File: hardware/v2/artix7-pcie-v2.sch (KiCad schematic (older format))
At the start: 43 parts, among them J10 USB_B_Micro, J3 JTAG_EN, J6 JTAG, J7 Conn_01x02, J8 SER, SW1 PROG, SW2 SW_SPST, U1 XC7A75T-FGG484, U2 W25Q64JVSSIM, U4 5P49V6965A000NLGI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

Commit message: v2 schematic/pcb progress commit - 12 unrouted
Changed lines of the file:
@@
 F13 "IO_L22_16_P" B R 10600 5300 50
 F14 "VCCO_16" I R 10600 5800 50
-F15 "IO_L23_16_N" B L 9350 5200 50
-F16 "IO_L23_16_P" B L 9350 5100 50
+F15 "IO_L9_16_N" B L 9350 5200 50
+F16 "IO_L9_16_P" B L 9350 5100 50
 $EndSheet
 Wire Wire Line
@@
 F40 "IO_L0_14" O R 10600 3850 50
 F41 "IO_L11_14_P" B L 9350 3750 50
-F42 "IO_L23_16_P" B L 9350 4750 50
-F43 "IO_L23_16_N" B L 9350 4650 50
+F42 "IO_L9_16_N" B L 9350 4650 50
+F43 "IO_L9_16_P" B L 9350 4750 50
 $EndSheet
 $Comp

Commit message: v2 hardware progress commit - fixed mounting holes and board edge
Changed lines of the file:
@@
 F19 "IO_L13_14_P" I R 10600 3150 50
 F20 "IO_L18_14_P" I L 9350 1600 50
-F21 "IO_L16_14_P" I R 10600 1600 50
-F22 "IO_L16_14_N" O R 10600 1500 50
-F23 "IO_L12_14_P" I R 10600 1800 50
-F24 "IO_L12_14_N" O R 10600 1700 50
-F25 "IO_L19_14_P" O L 9350 2900 50
-F26 "IO_L22_14_P" O L 9350 2700 50
-F27 "IO_L24_14_P" O L 9350 2500 50
-F28 "IO_L14_14_P" B L 9350 3550 50
-F29 "IO_L18_14_N" O L 9350 3250 50
-F30 "IO_L14_14_N" B L 9350 3650 50
-F31 "VCCO_14" I R 10600 2700 50
-F32 "VCCO_16" I R 10600 2800 50
-F33 "IO_L13_14_N" I R 10600 3250 50
-F34 "IO_L21_14_N" B R 10600 3550 50
-F35 "IO_L21_14_P" O R 10600 3450 50
-F36 "IO_L22_14_N" I L 9350 3950 50
-F37 "IO_L24_14_N" I L 9350 3850 50
-F38 "IO_L5_14_P" B R 10600 4150 50
-F39 "IO_L5_14_N" B R 10600 4050 50
-F40 "IO_L0_14" O R 10600 3850 50
-F41 "IO_L11_14_P" B L 9350 3750 50
-F42 "IO_L9_16_N" B L 9350 4650 50
-F43 "IO_L9_16_P" B L 9350 4750 50
+F21 "IO_L16_14_N" O R 10600 1500 50
+F22 "IO_L12_14_P" I R 10600 1800 50
+F23 "IO_L19_14_P" O L 9350 2900 50
+F24 "IO_L22_14_P" O L 9350 2700 50
+F25 "IO_L24_14_P" O L 9350 2500 50
+F26 "IO_L14_14_P" B L 9350 3550 50
+F27 "IO_L18_14_N" O L 9350 3250 50
+F28 "IO_L14_14_N" B L 9350 3650 50
+F29 "VCCO_14" I R 10600 2700 50
+F30 "VCCO_16" I R 10600 2800 50
+F31 "IO_L13_14_N" I R 10600 3250 50
+F32 "IO_L21_14_N" B R 10600 3550 50
+F33 "IO_L21_14_P" O R 10600 3450 50
+F34 "IO_L22_14_N" I L 9350 3950 50
+F35 "IO_L24_14_N" I L 9350 3850 50
+F36 "IO_L5_14_P" B R 10600 4150 50
+F37 "IO_L5_14_N" B R 10600 4050 50
+F38 "IO_L0_14" O R 10600 3850 50
+F39 "IO_L11_14_P" B L 9350 3750 50
+F40 "IO_L9_16_N" B L 9350 4650 50
+F41 "IO_L9_16_P" B L 9350 4750 50
+F42 "IO_L12_14_N" I R 10600 1700 50
+F43 "IO_L16_14_P" O R 10600 1600 50
 $EndSheet
 $Comp

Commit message: v2 hardware: J2 differential pairs tuned
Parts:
- SW2: value SW_SPST -> USER
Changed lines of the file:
@@
 P 8950 1800
 F 0 "SW2" H 8950 2035 50  0000 C CNN
-F 1 "SW_SPST" H 8950 1944 50  0000 C CNN
+F 1 "USER" H 8950 1944 50  0000 C CNN
 F 2 "tom-mechanical:SW_Push_1P1T_NO_CK_KMR2" H 8950 1800 50  0001 C CNN
 F 3 "~" H 8950 1800 50  0001 C CNN

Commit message: v2 hardware: j2_34 diff pairs matched, fix 0402 resistor packages, dropped paste from DNP resistors
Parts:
- R1, R10, R2, R29, R3, R30, R34, R35, R37, R4, R5, R51, R6, R7, R9: footprint tom-passives:C_0402_1005Metric -> tom-passives:R_0402_1005Metric
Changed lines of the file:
@@
 F 0 "R7" H 7971 1188 40  0000 L CNN
 F 1 "4.7k/5%" H 7971 1112 40  0000 L CNN
-F 2 "tom-passives:C_0402_1005Metric" V 7830 1150 30  0001 C CNN
+F 2 "tom-passives:R_0402_1005Metric" V 7830 1150 30  0001 C CNN
 F 3 "" H 7900 1150 30  0000 C CNN
 	1    7900 1150
@@
 F 0 "R6" H 6471 1088 40  0000 L CNN
 F 1 "2.4k/5%" H 6471 1012 40  0000 L CNN
-F 2 "tom-passives:C_0402_1005Metric" V 6330 1050 30  0001 C CNN
+F 2 "tom-passives:R_0402_1005Metric" V 6330 1050 30  0001 C CNN
 F 3 "" H 6400 1050 30  0000 C CNN
 	1    6400 1050
@@
 F 0 "R5" H 6071 988 40  0000 L CNN
 F 1 "4.7k/5%" H 6071 912 40  0000 L CNN
-F 2 "tom-passives:C_0402_1005Metric" V 5930 950 30  0001 C CNN
+F 2 "tom-passives:R_0402_1005Metric" V 5930 950 30  0001 C CNN
 F 3 "" H 6000 950 30  0000 C CNN
 	1    6000 950
@@
 F 0 "R3" H 5071 3088 40  0000 L CNN
 F 1 "4.7k/5%" H 5071 3012 40  0000 L CNN
-F 2 "tom-passives:C_0402_1005Metric" V 4930 3050 30  0001 C CNN
+F 2 "tom-passives:R_0402_1005Metric" V 4930 3050 30  0001 C CNN
 F 3 "" H 5000 3050 30  0000 C CNN
 	1    5000 3050
@@
 F 0 "R2" H 4671 2988 40  0000 L CNN
 F 1 "4.7k/5%" H 4671 2912 40  0000 L CNN
-F 2 "tom-passives:C_0402_1005Metric" V 4530 2950 30  0001 C CNN
+F 2 "tom-passives:R_0402_1005Metric" V 4530 2950 30  0001 C CNN
 F 3 "" H 4600 2950 30  0000 C CNN
 	1    4600 2950
@@
 F 0 "R1" H 4221 2888 40  0000 L CNN
 F 1 "1K/5%" H 4221 2812 40  0000 L CNN
-F 2 "tom-passives:C_0402_1005Metric" V 4080 2850 30  0001 C CNN
+F 2 "tom-passives:R_0402_1005Metric" V 4080 2850 30  0001 C CNN
 F 3 "" H 4150 2850 30  0000 C CNN
 	1    4150 2850
@@
 F 0 "R4" H 5921 2488 40  0000 L CNN
 F 1 "1k/5%" H 5921 2412 40  0000 L CNN
-F 2 "tom-passives:C_0402_1005Metric" V 5780 2450 30  0001 C CNN
+F 2 "tom-passives:R_0402_1005Metric" V 5780 2450 30  0001 C CNN
 F 3 "" H 5850 2450 30  0000 C CNN
 	1    5850 2450
@@
 F 0 "R30" V 8765 2500 40  0000 C CNN
 F 1 "1k/5%" V 8841 2500 40  0000 C CNN
-F 2 "tom-passives:C_0402_1005Metric" V 8880 2500 30  0001 C CNN
+F 2 "tom-passives:R_0402_1005Metric" V 8880 2500 30  0001 C CNN
 F 3 "" H 8950 2500 30  0000 C CNN
 	1    8950 2500
@@
 F 0 "R29" H 5779 6662 40  0000 R CNN
 F 1 "1.5k" H 5779 6738 40  0000 R CNN
-F 2 "tom-passives:C_0402_1005Metric" V 5780 6700 30  0001 C CNN
+F 2 "tom-passives:R_0402_1005Metric" V 5780 6700 30  0001 C CNN
 F 3 "" H 5850 6700 30  0001 C CNN
 	1    5850 6700
@@
 F 0 "R34" V 8850 2700 40  0000 C CNN
 F 1 "270R/5%" V 9050 2700 40  0000 C CNN
-F 2 "tom-passives:C_0402_1005Metric" V 8880 2700 30  0001 C CNN
+F 2 "tom-passives:R_0402_1005Metric" V 8880 2700 30  0001 C CNN
 F 3 "" H 8950 2700 30  0000 C CNN
 	1    8950 2700
@@
 F 0 "R35" V 9050 2900 40  0000 C CNN
 F 1 "270R/5%" V 9150 2900 40  0000 C CNN
-F 2 "tom-passives:C_0402_1005Metric" V 8880 2900 30  0001 C CNN
+F 2 "tom-passives:R_0402_1005Metric" V 8880 2900 30  0001 C CNN
 F 3 "" H 8950 2900 30  0000 C CNN
 	1    8950 2900
@@
 F 0 "R37" V 9050 3300 40  0000 R CNN
 F 1 "1.5k" V 8850 3300 40  0000 R CNN
-F 2 "tom-passives:C_0402_1005Metric" V 8880 3250 30  0001 C CNN
+F 2 "tom-passives:R_0402_1005Metric" V 8880 3250 30  0001 C CNN
 F 3 "" H 8950 3250 30  0001 C CNN
 	1    8950 3250
@@
 F 0 "R10" H 1271 5188 40  0000 L CNN
 F 1 "10K/5%" H 1271 5112 40  0000 L CNN
-F 2 "tom-passives:C_0402_1005Metric" V 1130 5150 30  0001 C CNN
+F 2 "tom-passives:R_0402_1005Metric" V 1130 5150 30  0001 C CNN
 F 3 "" H 1200 5150 30  0000 C CNN
 	1    1200 5150
@@
 F 0 "R9" H 1121 5188 40  0000 L CNN
 F 1 "10K/5%" H 1121 5112 40  0000 L CNN
-F 2 "tom-passives:C_0402_1005Metric" V 980 5150 30  0001 C CNN
+F 2 "tom-passives:R_0402_1005Metric" V 980 5150 30  0001 C CNN
 F 3 "" H 1050 5150 30  0000 C CNN
 	1    1050 5150
@@
 F 0 "R51" H 6471 5238 40  0000 L CNN
 F 1 "1K/5%" H 6471 5162 40  0000 L CNN
-F 2 "tom-passives:C_0402_1005Metric" V 6330 5200 30  0001 C CNN
+F 2 "tom-passives:R_0402_1005Metric" V 6330 5200 30  0001 C CNN
 F 3 "" H 6400 5200 30  0000 C CNN
 	1    6400 5200

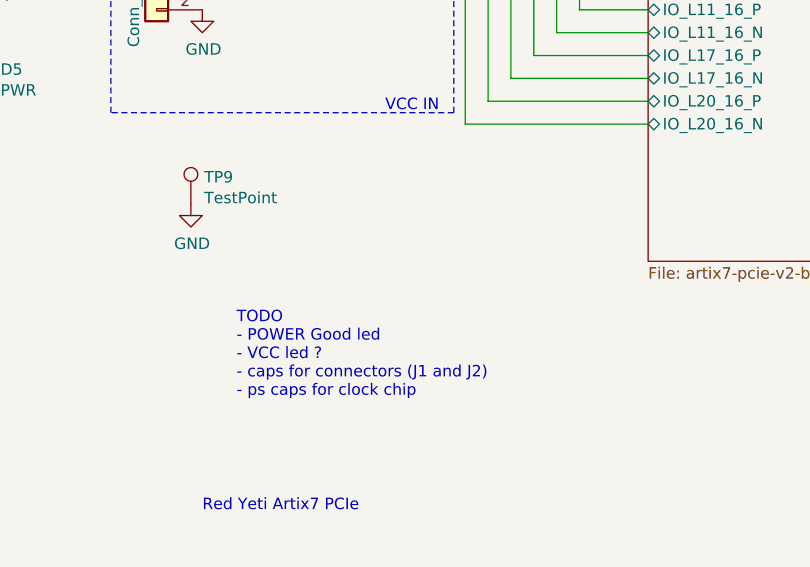
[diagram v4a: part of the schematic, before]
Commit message: v2 hardware : add missing mounting holes, all pairs tuned and passing. J1_34_DP0.5/0.5 -> MEETS INTER-PAIR TOLERANCE 0.5000 mm (current delta 0.4093)     /artix7-pcie-v2-bank34/IO_L1_34 meets intra-pair tolerance 0.5000 mm (current delta 0.0001)     /artix7-pcie-v2-bank34/IO_L2_34 meets intra-pair tolerance 0.5000 mm (current delta 0.0740)     /artix7-pcie-v2-bank34/IO_L3_34 meets intra-pair tolerance 0.5000 mm (current delta 0.0001)     /artix7-pcie-v2-bank34/IO_L4_34 meets intra-pair tolerance 0.5000 mm (current delta 0.0799)     /artix7-pcie-v2-bank34/IO_L5_34 meets intra-pair tolerance 0.5000 mm (current delta 0.0000)     /artix7-pcie-v2-bank34/IO_L7_34 meets intra-pair tolerance 0.5000 mm (current delta 0.0000)     /artix7-pcie-v2-bank34/IO_L8_34 meets intra-pair tolerance 0.5000 mm (current delta 0.0465) J1_35_DP0.5/0.5 -> MEETS INTER-PAIR TOLERANCE 0.5000 mm (current delta 0.1851)     /artix7-pcie-v2-bank34/IO_L15_35 meets intra-pair tolerance 0.5000 mm (current delta 0.0000)     /artix7-pcie-v2-bank34/IO_L1_35 meets intra-pair tolerance 0.5000 mm (current delta 0.0000)     /artix7-pcie-v2-bank34/IO_L22_35 meets intra-pair tolerance 0.5000 mm (current delta 0.0000)     /artix7-pcie-v2-bank34/IO_L3_35 meets intra-pair tolerance 0.5000 mm (current delta 0.0000)     /artix7-pcie-v2-bank34/IO_L5_35 meets intra-pair tolerance 0.5000 mm (current delta 0.0000)     /artix7-pcie-v2-bank34/IO_L7_35 meets intra-pair tolerance 0.5000 mm (current delta 0.0000)     /artix7-pcie-v2-bank34/IO_L9_35 meets intra-pair tolerance 0.5000 mm (current delta 0.0000) J2_14_DP0.5/0.5 -> MEETS INTER-PAIR TOLERANCE 0.5000 mm (current delta 0.4675)     /artix7-pcie-v2-bank14/IO_L10_14 meets intra-pair tolerance 0.5000 mm (current delta 0.0304)     /artix7-pcie-v2-bank14/IO_L15_14 meets intra-pair tolerance 0.5000 mm (current delta 0.0001)     /artix7-pcie-v2-bank14/IO_L17_14 meets intra-pair tolerance 0.5000 mm (current delta 0.0001)     /artix7-pcie-v2-bank14/IO_L4_14 meets intra-pair to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
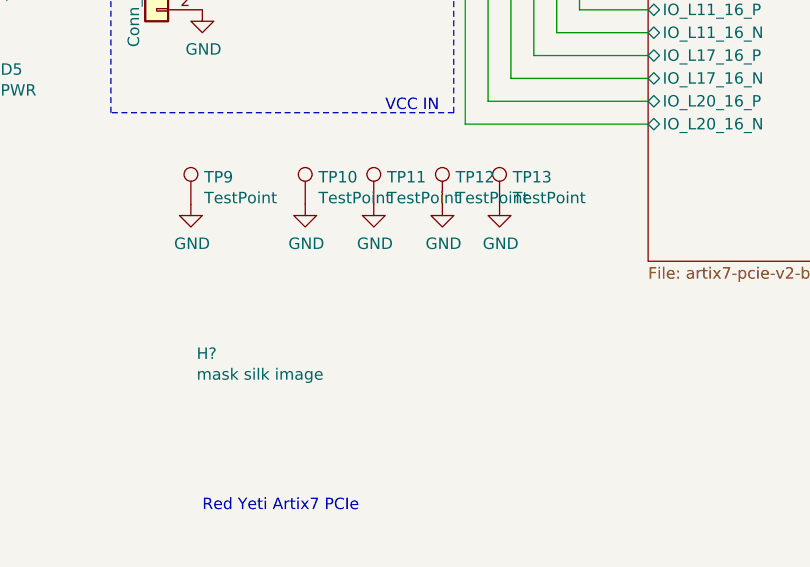
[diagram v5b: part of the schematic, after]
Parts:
- added H?: mask silk image, artix7-pcie-v2:mask, symbol tom-mechanical:mech-only-no-pins
- added TP10, TP11, TP12, TP13: TestPoint, tom-mechanical:MountingHole_2.7mm_M2.5_DIN965_Pad, symbol tom-mechanical:TestPoint
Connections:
- net GND: now also TP10.1, TP11.1, TP12.1, TP13.1
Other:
- note removed: "TODO \n- POWER Good led\n- VCC led ?\n- caps for connectors (J1 and J2)\n- ps caps for clock chip"
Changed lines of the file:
@@
 	1    0    0    -1
 $EndComp
-Text Notes 7550 7000 0    50   ~ 0
-TODO \n- POWER Good led\n- VCC led ?\n- caps for connectors (J1 and J2)\n- ps caps for clock chip
 Wire Wire Line
 	9250 4750 9250 5100
@@
 EndData
 $EndBitmap
+$Comp
+L tom-mechanical:TestPoint TP10
+U 1 1 5EA0EA64
+P 7850 6150
+F 0 "TP10" H 7908 6268 50  0000 L CNN
+F 1 "TestPoint" H 7908 6177 50  0000 L CNN
+F 2 "tom-mechanical:MountingHole_2.7mm_M2.5_DIN965_Pad" H 8050 6150 50  0001 C CNN
+F 3 "~" H 8050 6150 50  0001 C CNN
+	1    7850 6150
+	1    0    0    -1
+$EndComp
+$Comp
+L tom-mechanical:TestPoint TP11
+U 1 1 5EA116C9
+P 8150 6150
+F 0 "TP11" H 8208 6268 50  0000 L CNN
+F 1 "TestPoint" H 8208 6177 50  0000 L CNN
+F 2 "tom-mechanical:MountingHole_2.7mm_M2.5_DIN965_Pad" H 8350 6150 50  0001 C CNN
+F 3 "~" H 8350 6150 50  0001 C CNN
+	1    8150 6150
+	1    0    0    -1
+$EndComp
+$Comp
+L tom-mechanical:TestPoint TP12
+U 1 1 5EA1194B
+P 8450 6150
+F 0 "TP12" H 8508 6268 50  0000 L CNN
+F 1 "TestPoint" H 8508 6177 50  0000 L CNN
+F 2 "tom-mechanical:MountingHole_2.7mm_M2.5_DIN965_Pad" H 8650 6150 50  0001 C CNN
+F 3 "~" H 8650 6150 50  0001 C CNN
+	1    8450 6150
+	1    0    0    -1
+$EndComp
+$Comp
+L tom-mechanical:TestPoint TP13
+U 1 1 5EA11BCE
+P 8700 6150
+F 0 "TP13" H 8758 6268 50  0000 L CNN
+F 1 "TestPoint" H 8758 6177 50  0000 L CNN
+F 2 "tom-mechanical:MountingHole_2.7mm_M2.5_DIN965_Pad" H 8900 6150 50  0001 C CNN
+F 3 "~" H 8900 6150 50  0001 C CNN
+	1    8700 6150
+	1    0    0    -1
+$EndComp
+$Comp
+L power:GND #PWR0154
+U 1 1 5EA1220C
+P 7850 6150
+F 0 "#PWR0154" H 7850 5900 50  0001 C CNN
+F 1 "GND" H 7855 5977 50  0000 C CNN
+F 2 "" H 7850 6150 50  0001 C CNN
+F 3 "" H 7850 6150 50  0001 C CNN
+	1    7850 6150
+	1    0    0    -1
+$EndComp
+$Comp
+L power:GND #PWR0155
+U 1 1 5EA12460
+P 8150 6150
+F 0 "#PWR0155" H 8150 5900 50  0001 C CNN
+F 1 "GND" H 8155 5977 50  0000 C CNN
+F 2 "" H 8150 6150 50  0001 C CNN
+F 3 "" H 8150 6150 50  0001 C CNN
+	1    8150 6150
+	1    0    0    -1
+$EndComp
+$Comp
+L power:GND #PWR0156
+U 1 1 5EA1265F
+P 8450 6150
+F 0 "#PWR0156" H 8450 5900 50  0001 C CNN
+F 1 "GND" H 8455 5977 50  0000 C CNN
+F 2 "" H 8450 6150 50  0001 C CNN
+F 3 "" H 8450 6150 50  0001 C CNN
+	1    8450 6150
+	1    0    0    -1
+$EndComp
+$Comp
+L power:GND #PWR0157
+U 1 1 5EA128CE
+P 8700 6150
+F 0 "#PWR0157" H 8700 5900 50  0001 C CNN
+F 1 "GND" H 8705 5977 50  0000 C CNN
+F 2 "" H 8700 6150 50  0001 C CNN
+F 3 "" H 8700 6150 50  0001 C CNN
+	1    8700 6150
+	1    0    0    -1
+$EndComp
+$Comp
+L tom-mechanical:mech-only-no-pins H?
+U 1 1 5EA59A1F
+P 7350 6850
+F 0 "H?" H 7375 6896 50  0000 L CNN
+F 1 "mask silk image" H 7375 6805 50  0000 L CNN
+F 2 "artix7-pcie-v2:mask" H 7350 6850 50  0001 C CNN
+F 3 "" H 7350 6850 50  0001 C CNN
+	1    7350 6850
+	1    0    0    -1
+$EndComp
 $EndSCHEMATC

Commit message: Apr2020 rc1
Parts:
- added R52: 100R/1%, tom-passives:R_0402_1005Metric, symbol tom-passives:R
- added TP14: SCL, tom-mechanical:TestPoint_Pad_D1.5mm, symbol tom-mechanical:TestPoint
- added TP15: SDA, tom-mechanical:TestPoint_Pad_D1.5mm, symbol tom-mechanical:TestPoint
- gave numbers to parts that had none: 1
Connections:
- net CLKIN_N: now also R52.2
- net CLKIN_P: now also R52.1
- net CLK_SCL: now also TP14.1
- net CLK_SDA: now also TP15.1
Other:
- moved on the sheet: C40, C41
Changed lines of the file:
@@
 Connection ~ 1200 5800
 Wire Wire Line
-	1200 5800 900  5800
+	1200 5800 650  5800
 Wire Wire Line
 	1050 5400 1050 5900
 Connection ~ 1050 5900
 Wire Wire Line
-	1050 5900 900  5900
-Text Label 900  5800 1    50   ~ 0
+	1050 5900 850  5900
+Text Label 600  5800 1    50   ~ 0
 CLK_SCL
-Text Label 900  5900 3    50   ~ 0
+Text Label 600  5900 3    50   ~ 0
 CLK_SDA
 $Comp
@@
 L tom-passives:C C?
 U 1 1 5EA5C2D9
-P 3400 5750
+P 3500 5950
 AR Path="/5E98B37D/5EA5C2D9" Ref="C?"  Part="1"
 AR Path="/5EA5C2D9" Ref="C41"  Part="1"
-F 0 "C41" V 3171 5750 40  0000 C CNN
-F 1 "0.1uF/6.3V/X5R/PCIE" V 3247 5750 40  0000 C CNN
-F 2 "tom-passives:C_0402_1005Metric" H 3438 5600 30  0001 C CNN
-F 3 "" H 3400 5750 60  0001 C CNN
-	1    3400 5750
+F 0 "C41" V 3271 5950 40  0000 C CNN
+F 1 "0.1uF/6.3V/X5R/PCIE" V 3347 5950 40  0000 C CNN
+F 2 "tom-passives:C_0402_1005Metric" H 3538 5800 30  0001 C CNN
+F 3 "" H 3500 5950 60  0001 C CNN
+	1    3500 5950
 	-1   0    0    1
 $EndComp
@@
 L tom-passives:C C?
 U 1 1 5EA5CB84
-P 3300 5450
+P 3000 5950
 AR Path="/5E98B37D/5EA5CB84" Ref="C?"  Part="1"
 AR Path="/5EA5CB84" Ref="C40"  Part="1"
-F 0 "C40" V 3071 5450 40  0000 C CNN
-F 1 "0.1uF/6.3V/X5R/PCIE" V 3147 5450 40  0000 C CNN
-F 2 "tom-passives:C_0402_1005Metric" H 3338 5300 30  0001 C CNN
-F 3 "" H 3300 5450 60  0001 C CNN
-	1    3300 5450
+F 0 "C40" V 2771 5950 40  0000 C CNN
+F 1 "0.1uF/6.3V/X5R/PCIE" V 2847 5950 40  0000 C CNN
+F 2 "tom-passives:C_0402_1005Metric" H 3038 5800 30  0001 C CNN
+F 3 "" H 3000 5950 60  0001 C CNN
+	1    3000 5950
 	-1   0    0    1
 $EndComp
 Wire Wire Line
-	3400 6400 3400 5950
-Wire Wire Line
-	3300 5650 3300 6300
-Wire Wire Line
-	3300 6300 2700 6300
-Wire Wire Line
-	3400 5550 3400 5150
-Wire Wire Line
-	3300 5250 3300 5150
-Text Label 3300 5150 1    50   ~ 0
+	3500 6400 3500 6150
+Wire Wire Line
+	3000 6150 3000 6300
+Wire Wire Line
+	3000 6300 2700 6300
+Wire Wire Line
+	3500 5750 3500 5250
+Wire Wire Line
+	3000 5750 3000 5250
+Text Label 3000 5150 1    50   ~ 0
 CLKIN_P
-Text Label 3400 5150 1    50   ~ 0
+Text Label 3500 5150 1    50   ~ 0
 CLKIN_N
 Text Label 2700 6300 0    50   ~ 0
@@
 	10800 1400 10800 1850
 Wire Wire Line
-	2700 6400 3400 6400
+	2700 6400 3500 6400
 $Comp
 L tom-mechanical:TestPoint TP9
@@
 $EndComp
 $Comp
-L tom-mechanical:mech-only-no-pins H?
+L tom-mechanical:mech-only-no-pins H1
 U 1 1 5EA59A1F
 P 7350 6850
-F 0 "H?" H 7375 6896 50  0000 L CNN
+F 0 "H1" H 7375 6896 50  0000 L CNN
 F 1 "mask silk image" H 7375 6805 50  0000 L CNN
 F 2 "artix7-pcie-v2:mask" H 7350 6850 50  0001 C CNN
@@
 	1    0    0    -1
 $EndComp
+$Comp
+L tom-passives:R R52
+U 1 1 5EB1B352
+P 3250 5250
+F 0 "R52" H 3321 5288 40  0000 L CNN
+F 1 "100R/1%" H 3321 5212 40  0000 L CNN
+F 2 "tom-passives:R_0402_1005Metric" V 3180 5250 30  0001 C CNN
+F 3 "" H 3250 5250 30  0000 C CNN
+	1    3250 5250
+	0    -1   -1   0
+$EndComp
+Connection ~ 3000 5250
+Wire Wire Line
+	3000 5250 3000 5150
+Connection ~ 3500 5250
+Wire Wire Line
+	3500 5250 3500 5150
+$Comp
+L tom-mechanical:TestPoint TP?
+U 1 1 5EBA7F24
+P 650 5800
+AR Path="/5E6D5E13/5EBA7F24" Ref="TP?"  Part="1"
+AR Path="/5EBA7F24" Ref="TP14"  Part="1"
+F 0 "TP14" H 708 5872 50  0000 L CNN
+F 1 "SCL" H 708 5827 50  0001 L CNN
+F 2 "tom-mechanical:TestPoint_Pad_D1.5mm" H 850 5800 50  0001 C CNN
+F 3 "~" H 850 5800 50  0001 C CNN
+	1    650  5800
+	1    0    0    -1
+$EndComp
+Connection ~ 650  5800
+Wire Wire Line
+	650  5800 600  5800
+$Comp
+L tom-mechanical:TestPoint TP?
+U 1 1 5EBBEE9A
+P 850 5600
+AR Path="/5E6D5E13/5EBBEE9A" Ref="TP?"  Part="1"
+AR Path="/5EBBEE9A" Ref="TP15"  Part="1"
+F 0 "TP15" H 908 5672 50  0000 L CNN
+F 1 "SDA" H 908 5627 50  0001 L CNN
+F 2 "tom-mechanical:TestPoint_Pad_D1.5mm" H 1050 5600 50  0001 C CNN
+F 3 "~" H 1050 5600 50  0001 C CNN
+	1    850  5600
+	1    0    0    -1
+$EndComp
+Wire Wire Line
+	850  5600 850  5900
+Connection ~ 850  5900
+Wire Wire Line
+	850  5900 600  5900
 $EndSCHEMATC
